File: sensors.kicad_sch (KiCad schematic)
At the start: 5 parts, among them J5 Conn_01x04, U8 MPU-9250

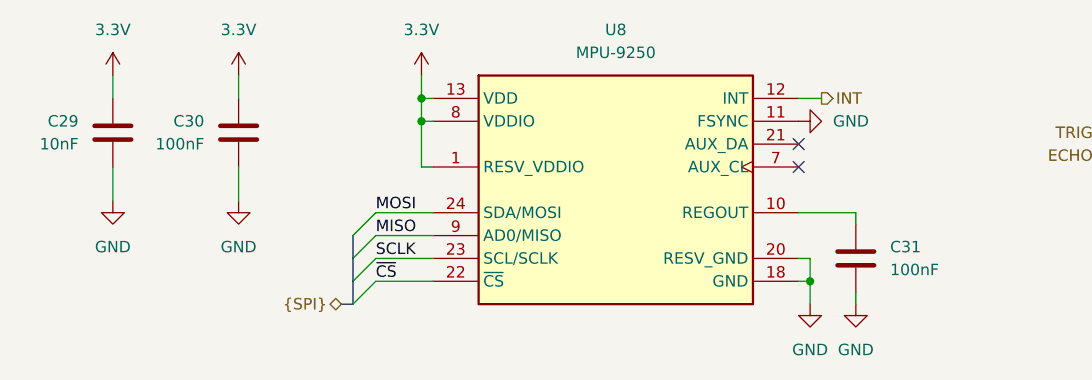
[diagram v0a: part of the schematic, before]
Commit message: Replace schottky with ideal diode
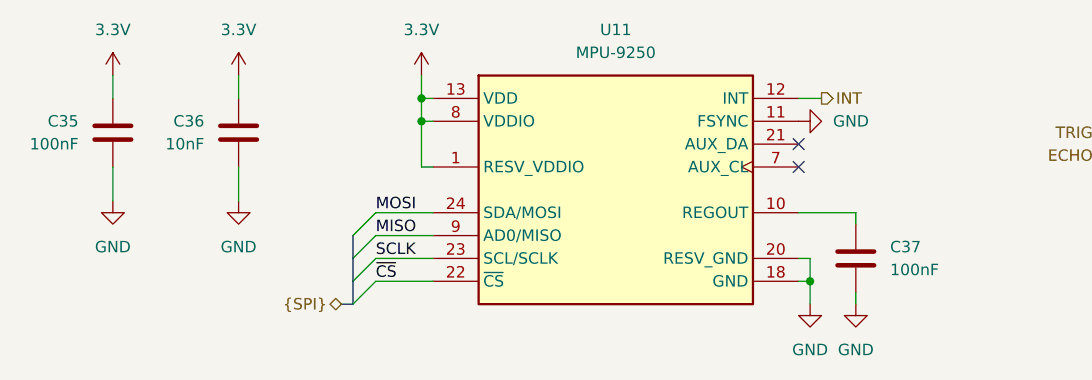
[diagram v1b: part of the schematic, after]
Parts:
- renumbered C30 to C35, C29 to C36, C31 to C37, U8 to U11
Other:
- moved on the sheet: C35, C36

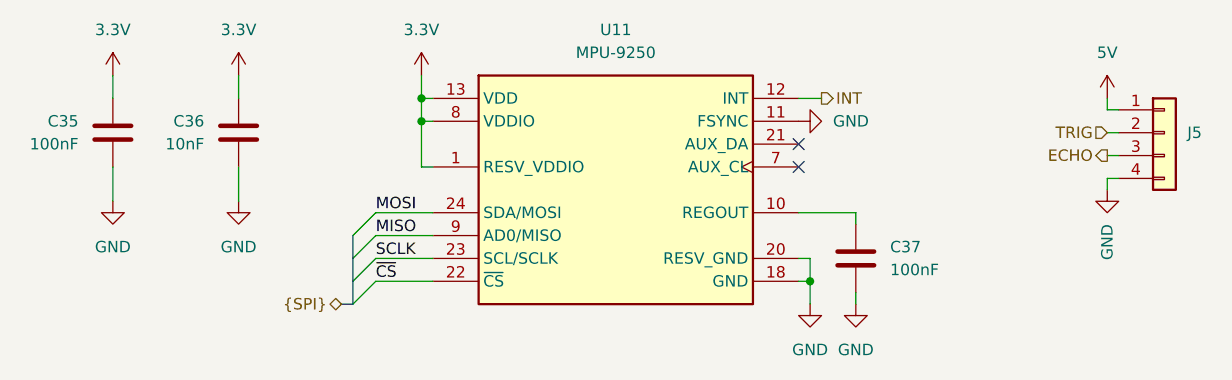
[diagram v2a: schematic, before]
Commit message: Follow DC-DC typical application
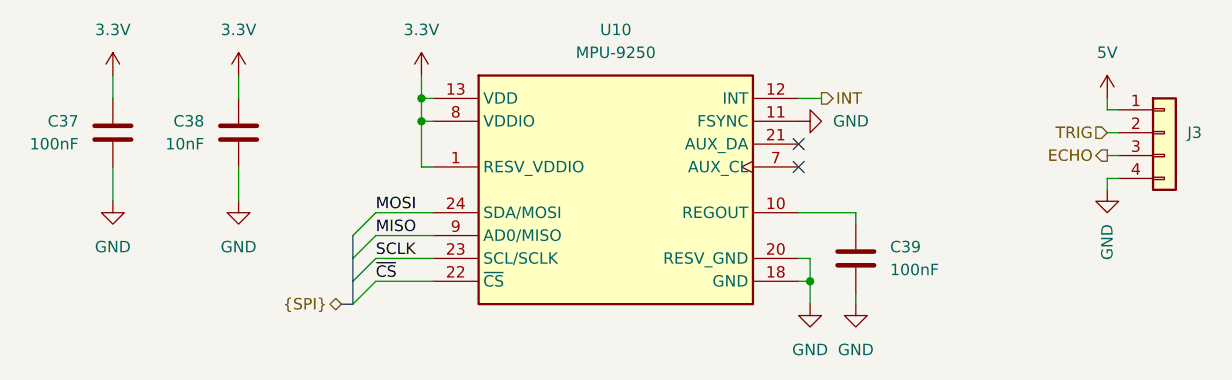
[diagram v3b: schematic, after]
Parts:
- renumbered C35 to C37, C36 to C38, C37 to C39, J5 to J3, U11 to U10
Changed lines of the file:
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@@
 		(on_board yes)
 		(dnp no)
-		(property "Reference" "J5"
+		(property "Reference" "J3"
 			(at 212.09 92.7099 0)
 			(effects
@@
 			(project "Tumbler2_Redesign"
 				(path "/f3fd8d79-9d35-4c04-811e-2697a2740958/38423c09-d546-4c9c-b674-750983dc8f27"
-					(reference "J5")
+					(reference "J3")
 					(unit 1)
 				)
@@
 		(on_board yes)
 		(dnp no)
-		(property "Reference" "U11"
+		(property "Reference" "U10"
 			(at 148.59 81.28 0)
 			(effects
@@
 			(project "Tumbler2_Redesign"
 				(path "/f3fd8d79-9d35-4c04-811e-2697a2740958/38423c09-d546-4c9c-b674-750983dc8f27"
-					(reference "U11")
+					(reference "U10")
 					(unit 1)
 				)
@@
 		(dnp no)
 		(fields_autoplaced yes)
-		(property "Reference" "#PWR0115"
+		(property "Reference" "#PWR0118"
 			(at 92.71 90.17 0)
 			(effects
@@
 			(project "Tumbler2_Redesign"
 				(path "/f3fd8d79-9d35-4c04-811e-2697a2740958/38423c09-d546-4c9c-b674-750983dc8f27"
-					(reference "#PWR0115")
+					(reference "#PWR0118")
 					(unit 1)
 				)
@@
 		(dnp no)
 		(fields_autoplaced yes)
-		(property "Reference" "#PWR0116"
+		(property "Reference" "#PWR0119"
 			(at 106.68 90.17 0)
 			(effects
@@
 			(project "Tumbler2_Redesign"
 				(path "/f3fd8d79-9d35-4c04-811e-2697a2740958/38423c09-d546-4c9c-b674-750983dc8f27"
-					(reference "#PWR0116")
+					(reference "#PWR0119")
 					(unit 1)
 				)
@@
 		(dnp no)
 		(fields_autoplaced yes)
-		(property "Reference" "#PWR0122"
+		(property "Reference" "#PWR0125"
 			(at 106.68 106.68 0)
 			(effects
@@
 			(project "Tumbler2_Redesign"
 				(path "/f3fd8d79-9d35-4c04-811e-2697a2740958/38423c09-d546-4c9c-b674-750983dc8f27"
-					(reference "#PWR0122")
+					(reference "#PWR0125")
 					(unit 1)
 				)
@@
 		(dnp no)
 		(fields_autoplaced yes)
-		(property "Reference" "#PWR0121"
+		(property "Reference" "#PWR0124"
 			(at 92.71 106.68 0)
 			(effects
@@
 			(project "Tumbler2_Redesign"
 				(path "/f3fd8d79-9d35-4c04-811e-2697a2740958/38423c09-d546-4c9c-b674-750983dc8f27"
-					(reference "#PWR0121")
+					(reference "#PWR0124")
 					(unit 1)
 				)
@@
 		(dnp no)
 		(fields_autoplaced yes)
-		(property "Reference" "C37"
+		(property "Reference" "C39"
 			(at 179.07 105.4099 0)
 			(effects
@@
 			(project "Tumbler2_Redesign"
 				(path "/f3fd8d79-9d35-4c04-811e-2697a2740958/38423c09-d546-4c9c-b674-750983dc8f27"
-					(reference "C37")
+					(reference "C39")
 					(unit 1)
 				)
@@
 		(dnp no)
 		(fields_autoplaced yes)
-		(property "Reference" "#PWR0117"
+		(property "Reference" "#PWR0120"
 			(at 127 90.17 0)
 			(effects
@@
 			(project "Tumbler2_Redesign"
 				(path "/f3fd8d79-9d35-4c04-811e-2697a2740958/38423c09-d546-4c9c-b674-750983dc8f27"
-					(reference "#PWR0117")
+					(reference "#PWR0120")
 					(unit 1)
 				)
@@
 		(on_board yes)
 		(dnp no)
-		(property "Reference" "C36"
+		(property "Reference" "C38"
 			(at 102.87 91.4399 0)
 			(effects
@@
 			(project "Tumbler2_Redesign"
 				(path "/f3fd8d79-9d35-4c04-811e-2697a2740958/38423c09-d546-4c9c-b674-750983dc8f27"
-					(reference "C36")
+					(reference "C38")
 					(unit 1)
 				)
@@
 		(dnp no)
 		(fields_autoplaced yes)
-		(property "Reference" "#PWR0124"
+		(property "Reference" "#PWR0127"
 			(at 175.26 118.11 0)
 			(effects
@@
 			(project "Tumbler2_Redesign"
 				(path "/f3fd8d79-9d35-4c04-811e-2697a2740958/38423c09-d546-4c9c-b674-750983dc8f27"
-					(reference "#PWR0124")
+					(reference "#PWR0127")
 					(unit 1)
 				)
@@
 		(on_board yes)
 		(dnp no)
-		(property "Reference" "#PWR0120"
+		(property "Reference" "#PWR0123"
 			(at 203.2 105.41 0)
 			(effects
@@
 			(project "Tumbler2_Redesign"
 				(path "/f3fd8d79-9d35-4c04-811e-2697a2740958/38423c09-d546-4c9c-b674-750983dc8f27"
-					(reference "#PWR0120")
+					(reference "#PWR0123")
 					(unit 1)
 				)
@@
 		(dnp no)
 		(fields_autoplaced yes)
-		(property "Reference" "#PWR0123"
+		(property "Reference" "#PWR0126"
 			(at 170.18 118.11 0)
 			(effects
@@
 			(project "Tumbler2_Redesign"
 				(path "/f3fd8d79-9d35-4c04-811e-2697a2740958/38423c09-d546-4c9c-b674-750983dc8f27"
-					(reference "#PWR0123")
+					(reference "#PWR0126")
 					(unit 1)
 				)
@@
 		(dnp no)
 		(fields_autoplaced yes)
-		(property "Reference" "#PWR0118"
+		(property "Reference" "#PWR0121"
 			(at 203.2 92.71 0)
 			(effects
@@
 			(project "Tumbler2_Redesign"
 				(path "/f3fd8d79-9d35-4c04-811e-2697a2740958/38423c09-d546-4c9c-b674-750983dc8f27"
-					(reference "#PWR0118")
+					(reference "#PWR0121")
 					(unit 1)
 				)
@@
 		(dnp no)
 		(fields_autoplaced yes)
-		(property "Reference" "#PWR0119"
+		(property "Reference" "#PWR0122"
 			(at 175.26 91.44 0)
 			(effects
@@
 			(project "Tumbler2_Redesign"
 				(path "/f3fd8d79-9d35-4c04-811e-2697a2740958/38423c09-d546-4c9c-b674-750983dc8f27"
-					(reference "#PWR0119")
+					(reference "#PWR0122")
 					(unit 1)
 				)
@@
 		(on_board yes)
 		(dnp no)
-		(property "Reference" "C35"
+		(property "Reference" "C37"
 			(at 88.9 91.4399 0)
 			(effects
@@
 			(project "Tumbler2_Redesign"
 				(path "/f3fd8d79-9d35-4c04-811e-2697a2740958/38423c09-d546-4c9c-b674-750983dc8f27"
-					(reference "C35")
-					(unit 1)
-				)
+					(reference "C37")
+					(unit 1)
+				)

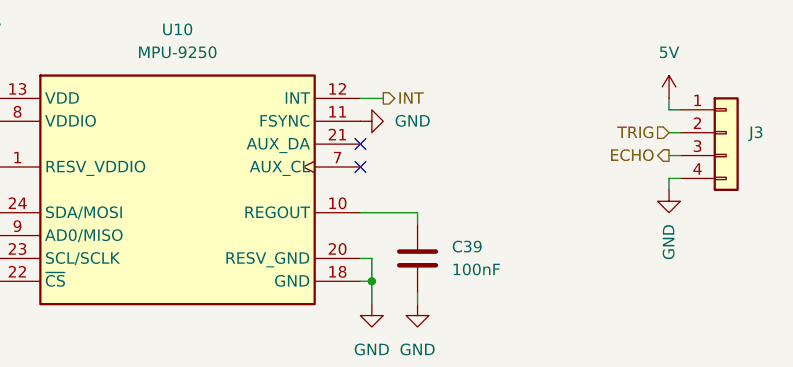
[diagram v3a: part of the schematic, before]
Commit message: Add test points
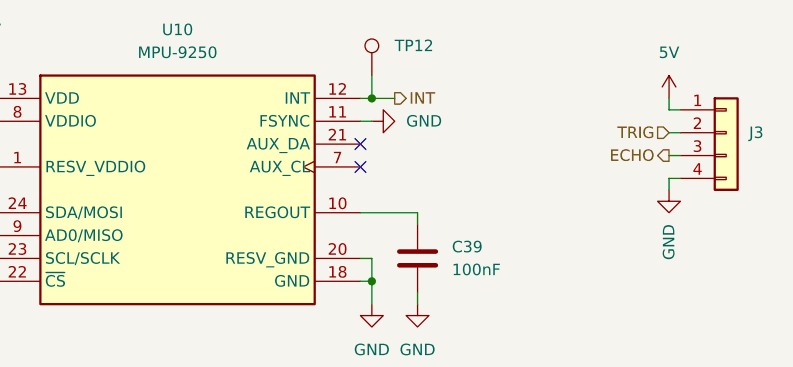
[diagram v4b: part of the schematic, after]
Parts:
- added TP12: TestPoint, symbol Connector:TestPoint
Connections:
- net INT: now also TP12.1
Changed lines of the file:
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@@
+	)
+	(junction
+		(at 170.18 88.9)
+		(diameter 0)
+		(color 0 0 0 0)
 	)
 	(junction
@@
 		)
 	)
+	(wire
+		(pts
+			(xy 170.18 86.36) (xy 170.18 88.9)
+		)
+		(stroke
+			(width 0)
+			(type default)
+		)
+	)
+	(wire
+		(pts
+			(xy 170.18 91.44) (xy 168.91 91.44)
+		)
+		(stroke
+			(width 0)
+			(type default)
+		)
+	)
 	(bus
 		(pts
@@
 	(wire
 		(pts
-			(xy 171.45 88.9) (xy 168.91 88.9)
+			(xy 172.72 88.9) (xy 170.18 88.9)
 		)
 		(stroke
@@
 		(pts
 			(xy 92.71 86.36) (xy 92.71 88.9)
+		)
+		(stroke
+			(width 0)
+			(type default)
+		)
+	)
+	(wire
+		(pts
+			(xy 170.18 88.9) (xy 168.91 88.9)
 		)
 		(stroke
@@
 	(hierarchical_label "INT"
 		(shape output)
-		(at 171.45 88.9 0)
+		(at 172.72 88.9 0)
 		(effects
 			(font
@@
 	)
 	(symbol
+		(lib_id "Connector:TestPoint")
+		(at 170.18 86.36 0)
+		(unit 1)
+		(exclude_from_sim no)
+		(in_bom yes)
+		(on_board yes)
+		(dnp no)
+		(fields_autoplaced yes)
+		(property "Reference" "TP12"
+			(at 172.72 83.0579 0)
+			(effects
+				(font
+					(size 1.27 1.27)
+				)
+				(justify left)
+			)
+		)
+		(property "Value" "TestPoint"
+			(at 167.64 81.7881 0)
+			(effects
+				(font
+					(size 1.27 1.27)
+				)
+				(justify right)
+				(hide yes)
+			)
+		)
+		(property "Footprint" ""
+			(at 175.26 86.36 0)
+			(effects
+				(font
+					(size 1.27 1.27)
+				)
+				(hide yes)
+			)
+		)
+		(property "Datasheet" "~"
+			(at 175.26 86.36 0)
+			(effects
+				(font
+					(size 1.27 1.27)
+				)
+				(hide yes)
+			)
+		)
+		(property "Description" "test point"
+			(at 170.18 86.36 0)
+			(effects
+				(font
+					(size 1.27 1.27)
+				)
+				(hide yes)
+			)
+		)
+		(pin "1"
+		)
+		(instances
+			(project "Tumbler2_Redesign"
+				(path "/f3fd8d79-9d35-4c04-811e-2697a2740958/38423c09-d546-4c9c-b674-750983dc8f27"
+					(reference "TP12")
+					(unit 1)
+				)
+			)
+		)
+	)
+	(symbol
 		(lib_id "power:GND")
 		(at 170.18 111.76 0)
@@
 	(symbol
 		(lib_id "power:GND")
-		(at 168.91 91.44 90)
+		(at 170.18 91.44 90)
 		(unit 1)
 		(exclude_from_sim no)
@@
 		(fields_autoplaced yes)
 		(property "Reference" "#PWR0122"
-			(at 175.26 91.44 0)
+			(at 176.53 91.44 0)
 			(effects
 				(font
@@
 		)
 		(property "Value" "GND"
-			(at 172.72 91.4399 90)
+			(at 173.99 91.4399 90)
 			(effects
 				(font
@@
 		)
 		(property "Footprint" ""
-			(at 168.91 91.44 0)
+			(at 170.18 91.44 0)
 			(effects
 				(font
@@
 		)
 		(property "Datasheet" ""
-			(at 168.91 91.44 0)
+			(at 170.18 91.44 0)
 			(effects
 				(font
@@
 		)
 		(property "Description" "Power symbol creates a global label with name \"GND\" , ground"
-			(at 168.91 91.44 0)
-			(effects
-				(font
+			(at 170.18 91.44 0)
+			(effects
+				(font

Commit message: Assign footprints
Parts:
- C37, C38, C39: footprint (none) -> Capacitor_SMD:C_0402_1005Metric_Pad0.74x0.62mm_HandSolder
- J3: footprint (none) -> Connector_PinHeader_2.54mm:PinHeader_1x04_P2.54mm_Vertical
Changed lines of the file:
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@@
 			)
 		)
-		(property "Footprint" ""
+		(property "Footprint" "Connector_PinHeader_2.54mm:PinHeader_1x04_P2.54mm_Vertical"
 			(at 209.55 92.71 0)
 			(effects
@@
 			)
 		)
-		(property "Footprint" ""
+		(property "Footprint" "Capacitor_SMD:C_0402_1005Metric_Pad0.74x0.62mm_HandSolder"
 			(at 176.2252 110.49 0)
 			(effects
@@
 			)
 		)
-		(property "Footprint" ""
+		(property "Footprint" "Capacitor_SMD:C_0402_1005Metric_Pad0.74x0.62mm_HandSolder"
 			(at 105.7148 96.52 0)
 			(effects
@@
 			)
 		)
-		(property "Footprint" ""
+		(property "Footprint" "Capacitor_SMD:C_0402_1005Metric_Pad0.74x0.62mm_HandSolder"
 			(at 91.7448 96.52 0)
 			(effects

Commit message: Assign LCSC part numbers
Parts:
- U10: LCSC Part (none) -> C71459
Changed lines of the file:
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@@
+			)
+		)
+		(property "LCSC Part" "C71459"
+			(at 148.59 99.06 0)
+			(effects
+				(font
+					(size 1.27 1.27)
+				)
+				(hide yes)
 			)
 		)

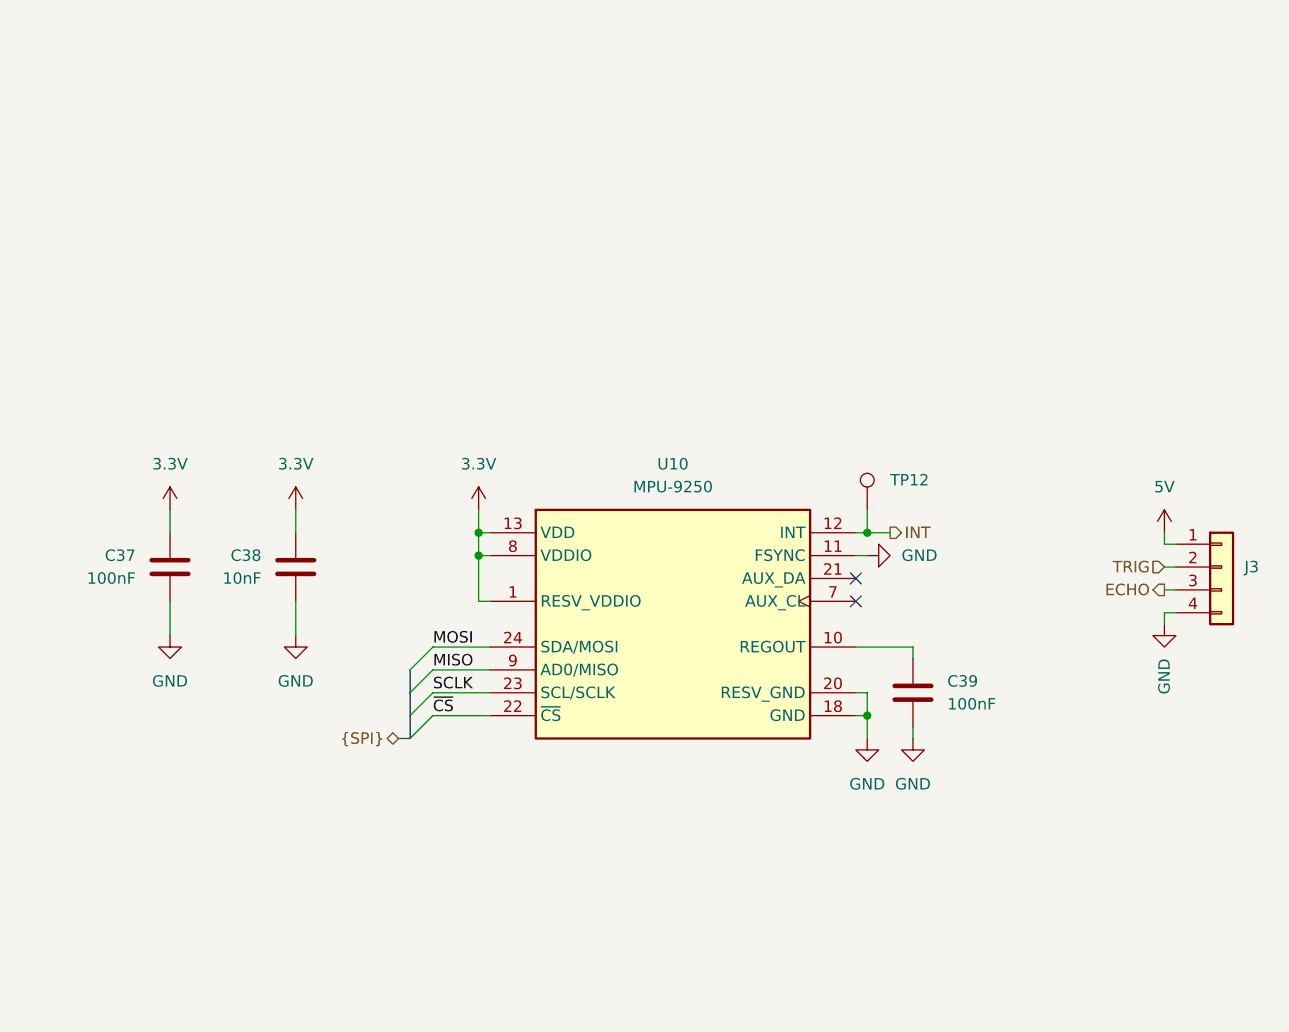
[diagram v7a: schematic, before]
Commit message: Prepare for IMU replacement
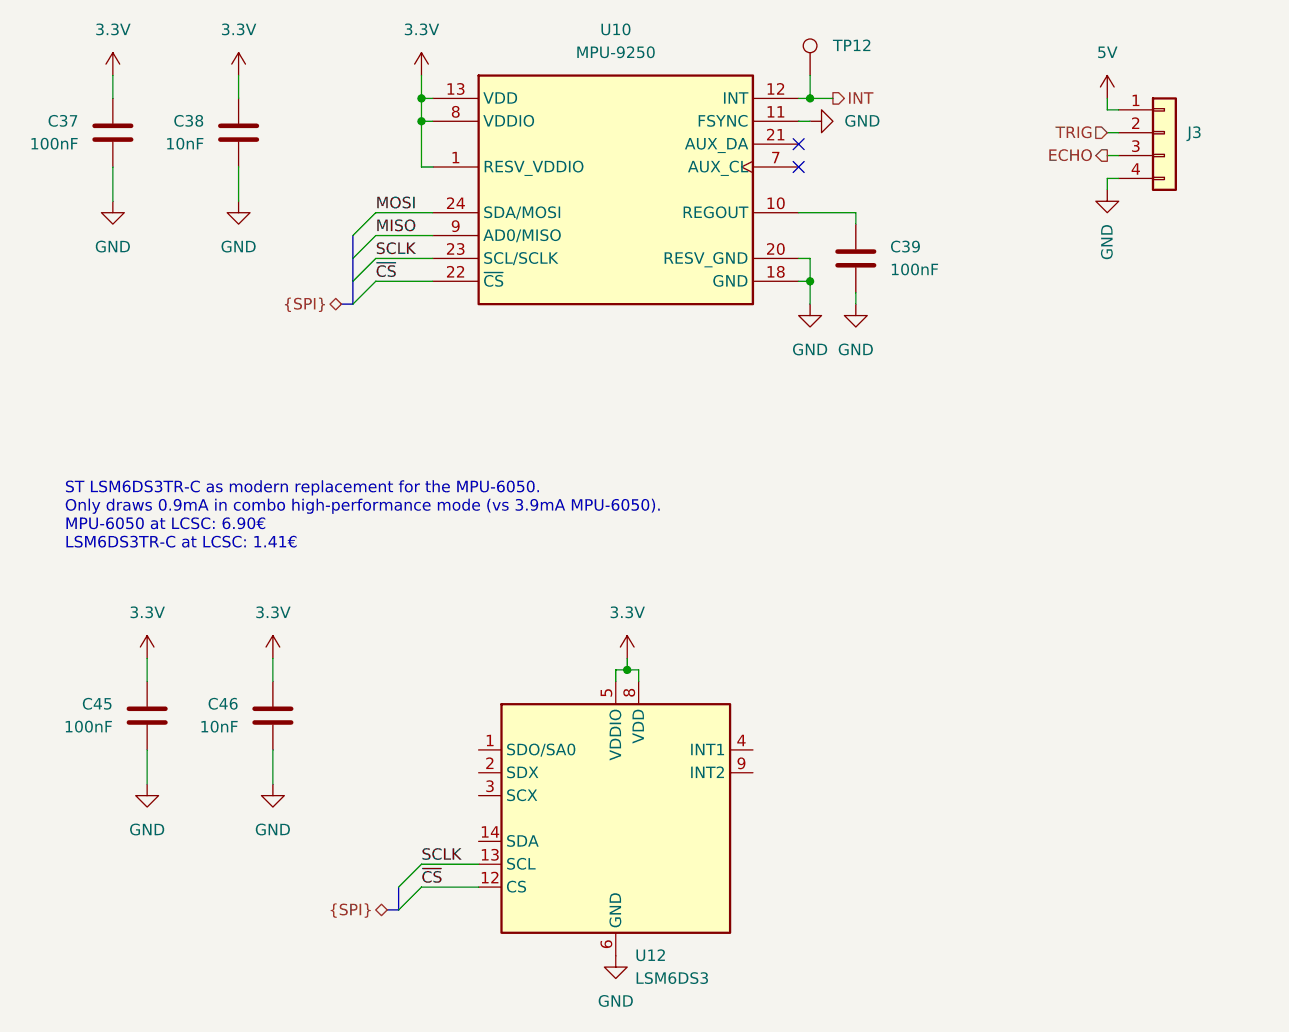
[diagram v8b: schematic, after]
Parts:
- added C45: 100nF, Capacitor_SMD:C_0402_1005Metric_Pad0.74x0.62mm_HandSolder, symbol Device:C
- added C46: 10nF, Capacitor_SMD:C_0402_1005Metric_Pad0.74x0.62mm_HandSolder, symbol Device:C
- added U12: LSM6DS3, Package_LGA:LGA-14_3x2.5mm_P0.5mm_LayoutBorder3x4y, symbol Sensor_Motion:LSM6DS3
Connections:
- net 3.3V: now also C45.1, C46.1, U12.5 (VDDIO), U12.8 (VDD)
- net GND: now also C45.2, C46.2, U12.6 (GND), U12.7 (GND)
- net SCLK: now also U12.13 (SCL)
- net ~{CS}: now also U12.12 (CS)
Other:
- note added: "ST LSM6DS3TR-C as modern replacement for the MPU-6050. Only draws 0.9mA in combo high-performance mode (vs 3.9mA MPU-6050). MPU-6050 at LCSC: 6.90€ LSM6DS3TR-C at LCSC: 1.41€"
- moved on the sheet: C37, C38, C39, J3, TP12, U10
